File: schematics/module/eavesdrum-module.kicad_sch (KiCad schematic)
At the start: 100 parts, among them J0 SUB-D 44 HD, J1 USB_A, J2 Conn_02x25_Odd_Even, J3 Conn_01x03, J4 Conn_01x20_Socket, J5 Conn_01x20_Socket, J7 DIN-5_180degree, SW1 SW_Push, SW2 SW_Push, SW3 SW_Push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

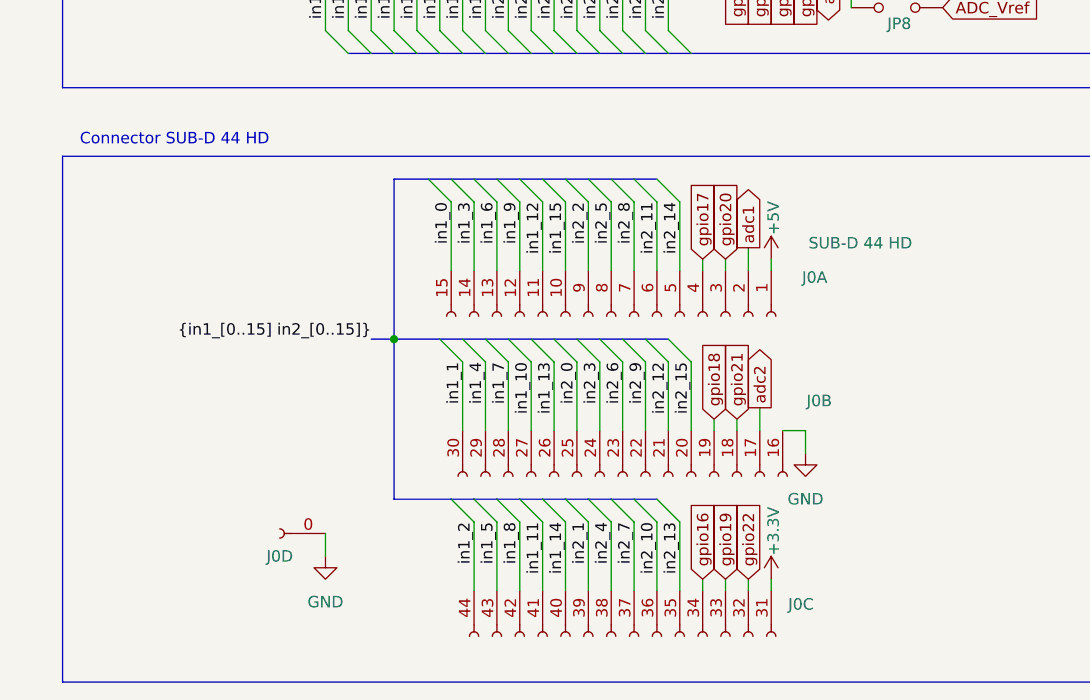
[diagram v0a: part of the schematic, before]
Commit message: minor schematic change
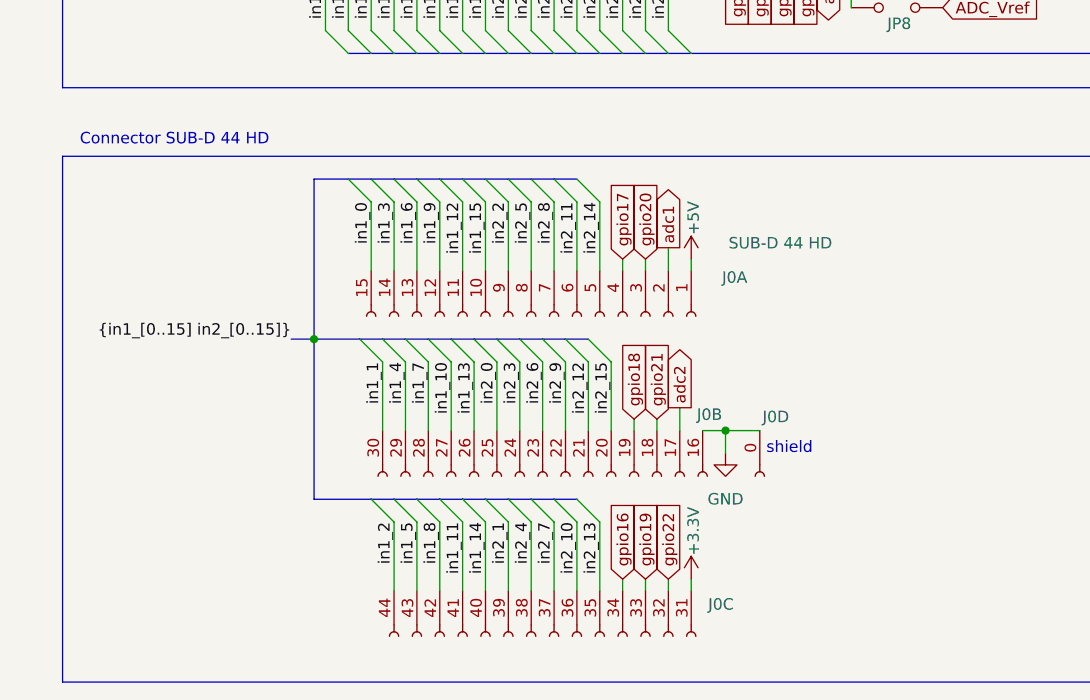
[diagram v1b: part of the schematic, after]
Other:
- note added: "shield"
- moved on the sheet: J0A, J0B, J0C, J0D
